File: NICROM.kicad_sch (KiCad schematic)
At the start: 6 parts, among them J5 Screw_Terminal_01x02, Q4 IRLZ44N

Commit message: Todo menos alimentación
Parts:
- removed D7: LED, LED_SMD:LED_0603_1608Metric, symbol Device:LED
- removed Q4: IRLZ44N, Package_TO_SOT_THT:TO-220-3_Horizontal_TabDown, symbol Transistor_FET:IRLZ44N
- removed R26: 100k, Resistor_SMD:R_0603_1608Metric, symbol Device:R_Small
- added Q1: IRLZ44NPBF, easyeda2kicad:TO-220-3_L10.0-W4.5-P2.54-T, symbol CANSAT_STM32_symbols:IRLZ44NPBF
- added R6: 100k, easyeda2kicad:R0603, symbol CANSAT_STM32_symbols:RC0603FR-07100KL
- added U9: Green LED, easyeda2kicad:LED0603-FD, symbol CANSAT_STM32_symbols:YLED0603G
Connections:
- net GND: now also Q1.3 (S), R6.1, U9.2 (-)
- net Led_Mosfet: now also U9.1 (+)
- net Mosfet_G: now also Q1.1 (G), R6.2
- net Mosfet_S: now also Q1.2 (D)
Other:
- note added: "BASICAMENTE CON ESTA RESISTENCIA SETEAS CUANTO QUIERES QUE PASE EL MOSFET soporta hasta 15A -- pista más ancha"

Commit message: BECERRA
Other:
- moved on the sheet: J5, Q1, R25, R27, R6, U9

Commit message: Cantidad de errores de la placa: 05
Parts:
- Q1: footprint easyeda2kicad:TO-220-3_L10.0-W4.5-P2.54-T -> ARLISS-footprints:TO-220-3_L10.0-W4.5-P2.54-T
- R6: footprint easyeda2kicad:R0603 -> ARLISS-footprints:R0603
- U9: footprint easyeda2kicad:LED0603-FD -> ARLISS-footprints:LED0603-FD
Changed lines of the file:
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@@
 			)
 		)
-		(property "Footprint" "easyeda2kicad:LED0603-FD"
+		(property "Footprint" "ARLISS-footprints:LED0603-FD"
 			(at 96.52 114.3 0)
 			(hide yes)
@@
 			)
 		)
-		(property "Footprint" "easyeda2kicad:R0603"
+		(property "Footprint" "ARLISS-footprints:R0603"
 			(at 130.81 110.49 0)
 			(hide yes)
@@
 			)
 		)
-		(property "Footprint" "easyeda2kicad:TO-220-3_L10.0-W4.5-P2.54-T"
+		(property "Footprint" "ARLISS-footprints:TO-220-3_L10.0-W4.5-P2.54-T"
 			(at 135.89 111.76 0)
 			(hide yes)

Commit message: Cantidad de errores en la placa: 04
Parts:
- J5: footprint TerminalBlock:TerminalBlock_bornier-2_P5.08mm -> TerminalBlock_RND:TerminalBlock_RND_205-00232_1x02_P5.08mm_Horizontal
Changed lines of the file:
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@@
 			)
 		)
-		(property "Footprint" "TerminalBlock:TerminalBlock_bornier-2_P5.08mm"
+		(property "Footprint" "TerminalBlock_RND:TerminalBlock_RND_205-00232_1x02_P5.08mm_Horizontal"
 			(at 143.51 80.01 0)
 			(hide yes)

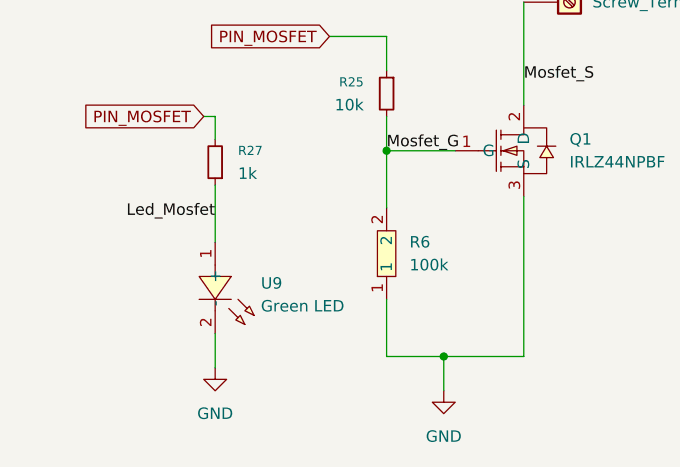
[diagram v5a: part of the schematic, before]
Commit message: Primer Ruteo de PCB
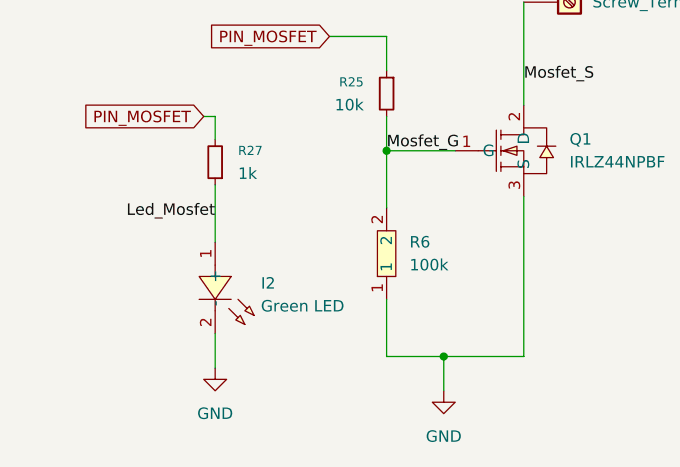
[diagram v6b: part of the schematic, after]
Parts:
- R25, R27: footprint Resistor_SMD:R_0603_1608Metric -> Capacitor_SMD:C_0603_1608Metric_Pad1.08x0.95mm_HandSolder
- renumbered U9 to I2
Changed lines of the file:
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@@
 			)
 		)
-		(property "Footprint" "Resistor_SMD:R_0603_1608Metric"
+		(property "Footprint" "Capacitor_SMD:C_0603_1608Metric_Pad1.08x0.95mm_HandSolder"
 			(at 104.14 100.33 0)
 			(hide yes)
@@
 			)
 		)
-		(property "Footprint" "Resistor_SMD:R_0603_1608Metric"
+		(property "Footprint" "Capacitor_SMD:C_0603_1608Metric_Pad1.08x0.95mm_HandSolder"
 			(at 123.19 92.71 0)
 			(hide yes)
@@
 		(dnp no)
 		(fields_autoplaced yes)
-		(property "Reference" "U9"
+		(property "Reference" "I2"
 			(at 109.22 113.7899 90)
 			(show_name no)
@@
 			(project "ARLISS_STM32_2026"
 				(path "/9719ea46-14c4-4409-9c57-49dd5454c03f/5b57be68-8372-451f-98b5-1e3ec0294f41"
-					(reference "U9")
+					(reference "I2")
 					(unit 1)
 				)

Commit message: Arreglos de esquemático
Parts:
- removed I2: Green LED, ARLISS-footprints:LED0603-FD, symbol CANSAT_STM32_symbols:YLED0603G
- R6: footprint ARLISS-footprints:R0603 -> Resistor_SMD:R_0603_1608Metric_Pad0.98x0.95mm_HandSolder
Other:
- moved on the sheet: R27
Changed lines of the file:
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@@
+	)
+	(junction
+		(at 90.17 105.41)
+		(diameter 0)
+		(color 0 0 0 0)
 	)
 	(junction
@@
 	(wire
 		(pts
-			(xy 104.14 97.79) (xy 104.14 95.25)
+			(xy 90.17 96.52) (xy 90.17 93.98)
 		)
 		(stroke
@@
 	(wire
 		(pts
-			(xy 104.14 109.22) (xy 104.14 102.87)
+			(xy 90.17 107.95) (xy 90.17 105.41)
 		)
 		(stroke
@@
 	(wire
 		(pts
-			(xy 102.87 95.25) (xy 104.14 95.25)
+			(xy 88.9 93.98) (xy 90.17 93.98)
 		)
 		(stroke
@@
 	(wire
 		(pts
-			(xy 138.43 121.92) (xy 129.54 121.92)
+			(xy 83.82 105.41) (xy 90.17 105.41)
 		)
 		(stroke
@@
 	(wire
 		(pts
-			(xy 138.43 82.55) (xy 138.43 93.98)
+			(xy 90.17 105.41) (xy 90.17 101.6)
 		)
 		(stroke
@@
 	(wire
 		(pts
-			(xy 123.19 121.92) (xy 129.54 121.92)
+			(xy 138.43 121.92) (xy 129.54 121.92)
 		)
 		(stroke
@@
 	(wire
 		(pts
-			(xy 116.84 86.36) (xy 123.19 86.36)
+			(xy 138.43 82.55) (xy 138.43 93.98)
 		)
 		(stroke
@@
 	(wire
 		(pts
-			(xy 104.14 119.38) (xy 104.14 123.19)
+			(xy 123.19 121.92) (xy 129.54 121.92)
+		)
+		(stroke
+			(width 0)
+			(type default)
+		)
+	)
+	(wire
+		(pts
+			(xy 116.84 86.36) (xy 123.19 86.36)
+		)
+		(stroke
+			(width 0)
+			(type default)
+		)
+	)
+	(wire
+		(pts
+			(xy 90.17 118.11) (xy 90.17 121.92)
 		)
 		(stroke
@@
 	)
 	(label "Led_Mosfet"
-		(at 104.14 106.68 180)
+		(at 83.82 105.41 180)
 		(effects
 			(font
@@
 	(global_label "PIN_MOSFET"
 		(shape input)
-		(at 102.87 95.25 180)
+		(at 88.9 93.98 180)
 		(fields_autoplaced yes)
 		(effects
@@
 		)
 		(property "Intersheetrefs" "${INTERSHEET_REFS}"
-			(at 88.5153 95.25 0)
+			(at 74.5453 93.98 0)
 			(hide yes)
 			(show_name no)
@@
 	(symbol
 		(lib_id "Device:R_Small")
-		(at 104.14 100.33 180)
+		(at 90.17 99.06 180)
 		(unit 1)
 		(body_style 1)
@@
 		(fields_autoplaced yes)
 		(property "Reference" "R27"
-			(at 106.68 99.0599 0)
+			(at 92.71 97.7899 0)
 			(show_name no)
 			(do_not_autoplace no)
@@
 		)
 		(property "Value" "1k"
-			(at 106.68 101.5999 0)
+			(at 92.71 100.3299 0)
 			(show_name no)
 			(do_not_autoplace no)
@@
 		)
 		(property "Footprint" "Capacitor_SMD:C_0603_1608Metric_Pad1.08x0.95mm_HandSolder"
-			(at 104.14 100.33 0)
+			(at 90.17 99.06 0)
 			(hide yes)
 			(show_name no)
@@
 		)
 		(property "Datasheet" ""
-			(at 104.14 100.33 0)
+			(at 90.17 99.06 0)
 			(hide yes)
 			(show_name no)
@@
 		)
 		(property "Description" "Resistor, small symbol"
-			(at 104.14 100.33 0)
+			(at 90.17 99.06 0)
 			(hide yes)
 			(show_name no)
@@
 		)
 		(property "Link" "https://www.lcsc.com/product-detail/C22548.html"
-			(at 104.14 100.33 90)
+			(at 90.17 99.06 90)
 			(hide yes)
 			(show_name no)
@@
 	)
 	(symbol
-		(lib_id "CANSAT_STM32_symbols:YLED0603G")
-		(at 105.41 114.3 270)
-		(unit 1)
-		(body_style 1)
-		(exclude_from_sim no)
-		(in_bom yes)
-		(on_board yes)
-		(in_pos_files yes)
-		(dnp no)
-		(fields_autoplaced yes)
-		(property "Reference" "I2"
-			(at 109.22 113.7899 90)
-			(show_name no)
-			(do_not_autoplace no)
-			(effects
-				(font
-					(size 1.27 1.27)
-				)
-				(justify left)
-			)
-		)
-		(property "Value" "Green LED"
-			(at 109.22 116.3299 90)
-			(show_name no)
-			(do_not_autoplace no)
-			(effects
-				(font
-					(size 1.27 1.27)
-				)
-				(justify left)
-			)
-		)
-		(property "Footprint" "ARLISS-footprints:LED0603-FD"
-			(at 96.52 114.3 0)
-			(hide yes)
-			(show_name no)
-			(do_not_autoplace no)
-			(effects
-				(font
-					(size 1.27 1.27)
-				)
-			)
-		)
-		(property "Datasheet" "https://www.lcsc.com/datasheet/C19273151.pdf"
-			(at 93.98 114.3 0)
-			(hide yes)
-			(show_name no)
-			(do_not_autoplace no)
-			(effects
-				(font
-					(size 1.27 1.27)
-				)
-			)
-		)
-		(property "Description" ""
-			(at 105.41 114.3 0)
-			(hide yes)
-			(show_name no)
-			(do_not_autoplace no)
-			(effects
-				(font
-					(size 1.27 1.27)
-				)
-			)
-		)
-		(property "Manufacturer" "YONGYUTAI(永裕泰)"
-			(at 91.44 114.3 0)
-			(hide yes)
-			(show_name no)
-			(do_not_autoplace no)
-			(effects
-				(font
-					(size 1.27 1.27)
-				)
-			)
-		)
-		(property "MPN" "YLED0603G"
-			(at 88.9 114.3 0)
-			(hide yes)
-			(show_name no)
-			(do_not_autoplace no)
-			(effects
-				(font
-					(size 1.27 1.27)
-				)
-			)
-		)
-		(property "LCSC Part" "C19273151"
-			(at 86.36 114.3 0)
-			(hide yes)
-			(show_name no)
-			(do_not_autoplace no)
-			(effects
-				(font
-					(size 1.27 1.27)
-				)
-			)
-		)
-		(pin "1"
-		)
-		(pin "2"
-		)
-		(instances
-			(project "ARLISS_STM32_2026"
-				(path "/9719ea46-14c4-4409-9c57-49dd5454c03f/5b57be68-8372-451f-98b5-1e3ec0294f41"
-					(reference "I2")
-					(unit 1)
-				)
-			)
-		)
-	)
-	(symbol
 		(lib_id "Connector:Screw_Terminal_01x02")
 		(at 143.51 80.01 0)
@@
 			)
 		)
-		(property "Footprint" "ARLISS-footprints:R0603"
+		(property "Footprint" "Resistor_SMD:R_0603_1608Metric_Pad0.98x0.95mm_HandSolder"
 			(at 130.81 110.49 0)
 			(hide yes)
@@
 	(symbol
 		(lib_id "power:GND")
-		(at 104.14 123.19 0)
+		(at 90.17 121.92 0)
 		(unit 1)
 		(body_style 1)
@@
 		(fields_autoplaced yes)
 		(property "Reference" "#PWR089"
-			(at 104.14 129.54 0)
+			(at 90.17 128.27 0)
 			(hide yes)
 			(show_name no)
@@
 		)
 		(property "Value" "GND"
-			(at 104.14 128.27 0)
+			(at 90.17 127 0)
 			(show_name no)
 			(do_not_autoplace no)
@@
 		)
 		(property "Footprint" ""
-			(at 104.14 123.19 0)
+			(at 90.17 121.92 0)
 			(hide yes)
 			(show_name no)
@@
 		)
 		(property "Datasheet" ""
-			(at 104.14 123.19 0)
+			(at 90.17 121.92 0)
 			(hide yes)
 			(show_name no)
@@
 		)
 		(property "Description" "Power symbol creates a global label with name \"GND\" , ground"
-			(at 104.14 123.19 0)
-			(hide yes)
-			(show_name no)
+			(at 90.17 121.92 0)
+			(hide yes)
+			(show_name no)

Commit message: Arreglando footprints
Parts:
- Q1: Manufacturer Infineon(英飞凌) -> (none)
- R19: renamed from R6; Manufacturer YAGEO(国巨) -> (none)
- renumbered J5 to J3, R27 to R17, R25 to R18
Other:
- company: (none) -> TOMEK TEAM
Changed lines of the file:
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@@
 	(generator_version "10.0")
 	(paper "A4")
+	(title_block
+		(company "TOMEK TEAM")
+	)
 	(text ""
 		(exclude_from_sim no)
@@
 		(dnp no)
 		(fields_autoplaced yes)
-		(property "Reference" "R27"
+		(property "Reference" "R17"
 			(at 92.71 97.7899 0)
 			(show_name no)
@@
 			(project "ARLISS_STM32_2026"
 				(path "/9719ea46-14c4-4409-9c57-49dd5454c03f/5b57be68-8372-451f-98b5-1e3ec0294f41"
-					(reference "R27")
+					(reference "R17")
 					(unit 1)
 				)
@@
 		(in_pos_files yes)
 		(dnp no)
-		(property "Reference" "R25"
+		(property "Reference" "R18"
 			(at 120.65 91.4399 0)
 			(show_name no)
@@
 			(project "ARLISS_STM32_2026"
 				(path "/9719ea46-14c4-4409-9c57-49dd5454c03f/5b57be68-8372-451f-98b5-1e3ec0294f41"
-					(reference "R25")
+					(reference "R18")
 					(unit 1)
 				)
@@
 		(dnp no)
 		(fields_autoplaced yes)
-		(property "Reference" "J5"
+		(property "Reference" "J3"
 			(at 146.05 80.0099 0)
 			(show_name no)
@@
 			(project "ARLISS_STM32_2026"
 				(path "/9719ea46-14c4-4409-9c57-49dd5454c03f/5b57be68-8372-451f-98b5-1e3ec0294f41"
-					(reference "J5")
+					(reference "J3")
 					(unit 1)
 				)
@@
 		(dnp no)
 		(fields_autoplaced yes)
-		(property "Reference" "R6"
+		(property "Reference" "R19"
 			(at 125.73 109.2199 90)
 			(show_name no)
@@
 		(property "Description" ""
 			(at 123.19 110.49 0)
-			(hide yes)
-			(show_name no)
-			(do_not_autoplace no)
-			(effects
-				(font
-					(size 1.27 1.27)
-				)
-			)
-		)
-		(property "Manufacturer" "YAGEO(国巨)"
-			(at 135.89 110.49 0)
 			(hide yes)
 			(show_name no)
@@
 			(project "ARLISS_STM32_2026"
 				(path "/9719ea46-14c4-4409-9c57-49dd5454c03f/5b57be68-8372-451f-98b5-1e3ec0294f41"
-					(reference "R6")
+					(reference "R19")
 					(unit 1)
 				)
@@
 			)
 		)
-		(property "Manufacturer" "Infineon(英飞凌)"
-			(at 135.89 116.84 0)
-			(hide yes)
-			(show_name no)
-			(do_not_autoplace no)
-			(effects
-				(font
-					(size 1.27 1.27)
-				)
-			)
-		)
 		(property "MPN" "IRLZ44NPBF"
 			(at 135.89 119.38 0)
@@
 		(dnp no)
 		(fields_autoplaced yes)
-		(property "Reference" "#PWR089"
+		(property "Reference" "#PWR0109"
 			(at 90.17 128.27 0)
 			(hide yes)
@@
 			(project "ARLISS_STM32_2026"
 				(path "/9719ea46-14c4-4409-9c57-49dd5454c03f/5b57be68-8372-451f-98b5-1e3ec0294f41"
-					(reference "#PWR089")
+					(reference "#PWR0109")
 					(unit 1)
 				)
@@
 		(in_pos_files yes)
 		(dnp no)
-		(property "Reference" "#PWR071"
+		(property "Reference" "#PWR0111"
 			(at 138.43 80.01 0)
 			(hide yes)
@@
 			(project "ARLISS_STM32_2026"
 				(path "/9719ea46-14c4-4409-9c57-49dd5454c03f/5b57be68-8372-451f-98b5-1e3ec0294f41"
-					(reference "#PWR071")
+					(reference "#PWR0111")
 					(unit 1)
 				)
@@
 		(dnp no)
 		(fields_autoplaced yes)
-		(property "Reference" "#PWR064"
+		(property "Reference" "#PWR0110"
 			(at 129.54 132.08 0)
 			(hide yes)
@@
 			(project "ARLISS_STM32_2026"
 				(path "/9719ea46-14c4-4409-9c57-49dd5454c03f/5b57be68-8372-451f-98b5-1e3ec0294f41"
-					(reference "#PWR064")
+					(reference "#PWR0110")
 					(unit 1)
 				)
